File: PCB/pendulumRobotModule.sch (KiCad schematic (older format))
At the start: 24 parts, among them J1 Conn_01x02_Female, J2 conn_3x4, J3 Conn_01x02_Male, J4 Conn_01x04_Female, J5 conn_3x3, J7 Conn_01x04_Female, U1 ESP32-devKit, U2 MPU6050-breakout, U3 buckConverter-adj

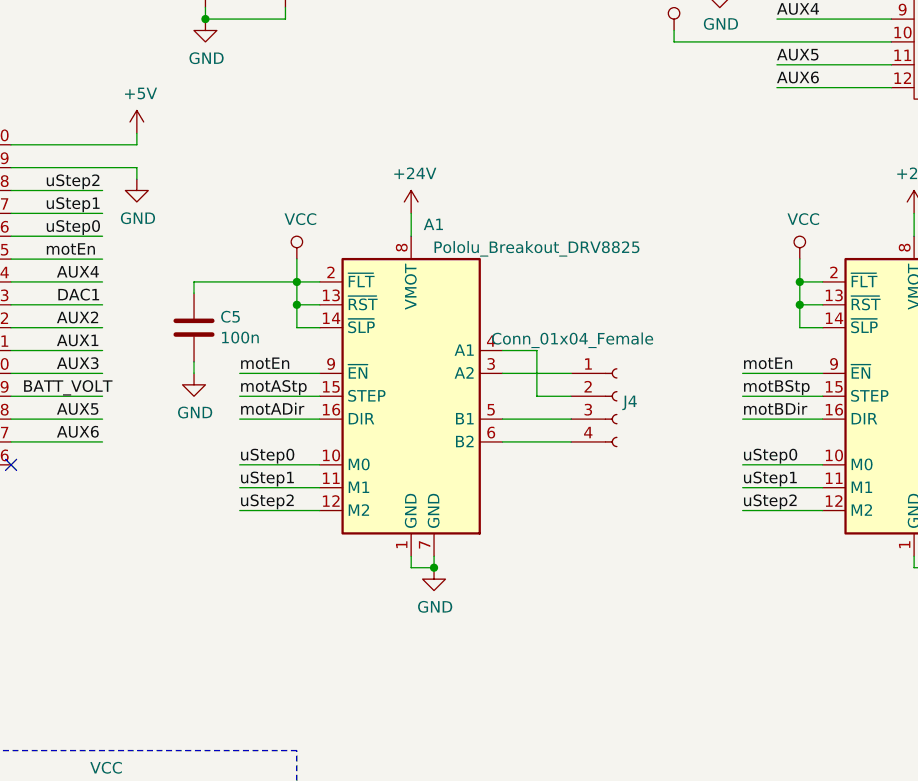
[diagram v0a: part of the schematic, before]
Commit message: PCB updates: increased 24V trace thickness, added a via (or rather added trace to via) in that signal, and added stepper motor enable pull-up to 3V3.
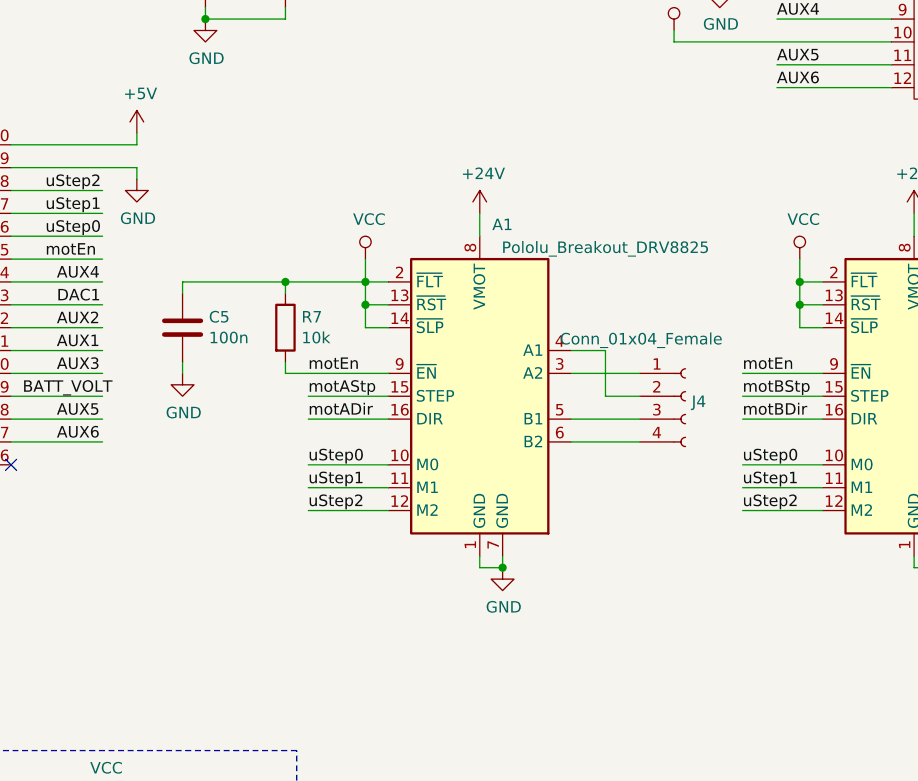
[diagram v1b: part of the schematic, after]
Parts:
- added R7: 10k, Resistors_SMD:R_0805_HandSoldering, symbol Device:R
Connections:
- wire segments 168 -> 171
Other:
- moved on the sheet: A1, C5, J4
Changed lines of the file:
@@
 L Driver_Motor:Pololu_Breakout_DRV8825 A1
 U 1 1 5BCC947E
-P 5500 4300
-F 0 "A1" H 5600 4950 50  0000 C CNN
-F 1 "Pololu_Breakout_DRV8825" H 6050 4850 50  0000 C CNN
-F 2 "mylib:DRV8825-breakout" H 5700 3500 50  0001 L CNN
-F 3 "https://www.pololu.com/product/2982" H 5600 4000 50  0001 C CNN
-	1    5500 4300
+P 5800 4300
+F 0 "A1" H 5900 4950 50  0000 C CNN
+F 1 "Pololu_Breakout_DRV8825" H 6350 4850 50  0000 C CNN
+F 2 "mylib:DRV8825-breakout" H 6000 3500 50  0001 L CNN
+F 3 "https://www.pololu.com/product/2982" H 5900 4000 50  0001 C CNN
+	1    5800 4300
 	1    0    0    -1
 $EndComp
@@
 L Connector:Conn_01x04_Female J4
 U 1 1 5BCCD4CD
-P 6400 4400
-F 0 "J4" H 6427 4376 50  0000 L CNN
-F 1 "Conn_01x04_Female" H 5850 4650 50  0000 L CNN
-F 2 "Socket_Strips:Socket_Strip_Straight_1x04_Pitch2.54mm" H 6400 4400 50  0001 C CNN
-F 3 "~" H 6400 4400 50  0001 C CNN
-	1    6400 4400
+P 6700 4400
+F 0 "J4" H 6727 4376 50  0000 L CNN
+F 1 "Conn_01x04_Female" H 6150 4650 50  0000 L CNN
+F 2 "Socket_Strips:Socket_Strip_Straight_1x04_Pitch2.54mm" H 6700 4400 50  0001 C CNN
+F 3 "~" H 6700 4400 50  0001 C CNN
+	1    6700 4400
 	1    0    0    -1
 $EndComp
@@
 	1    0    0    -1
 $EndComp
-Text Label 4750 4700 0    50   ~ 0
+Text Label 5050 4700 0    50   ~ 0
 uStep0
-Text Label 4750 4800 0    50   ~ 0
+Text Label 5050 4800 0    50   ~ 0
 uStep1
-Text Label 4750 4900 0    50   ~ 0
+Text Label 5050 4900 0    50   ~ 0
 uStep2
 Text Label 6950 4700 0    50   ~ 0
@@
 Text Label 6950 4300 0    50   ~ 0
 motEn
-Text Label 4750 4300 0    50   ~ 0
+Text Label 5050 4300 0    50   ~ 0
 motEn
 $Comp
 L power:GND #PWR0112
 U 1 1 5BD07181
-P 5600 5150
-F 0 "#PWR0112" H 5600 4900 50  0001 C CNN
-F 1 "GND" H 5605 4977 50  0000 C CNN
-F 2 "" H 5600 5150 50  0001 C CNN
-F 3 "" H 5600 5150 50  0001 C CNN
-	1    5600 5150
-	1    0    0    -1
-$EndComp
-Wire Wire Line
-	5500 5100 5500 5150
-Wire Wire Line
-	5500 5150 5600 5150
-Wire Wire Line
-	5600 5100 5600 5150
-Connection ~ 5600 5150
+P 5900 5150
+F 0 "#PWR0112" H 5900 4900 50  0001 C CNN
+F 1 "GND" H 5905 4977 50  0000 C CNN
+F 2 "" H 5900 5150 50  0001 C CNN
+F 3 "" H 5900 5150 50  0001 C CNN
+	1    5900 5150
+	1    0    0    -1
+$EndComp
+Wire Wire Line
+	5800 5100 5800 5150
+Wire Wire Line
+	5800 5150 5900 5150
+Wire Wire Line
+	5900 5100 5900 5150
+Connection ~ 5900 5150
 $Comp
 L power:GND #PWR0113
@@
 L power:+24V #PWR0114
 U 1 1 5BD122E8
-P 5500 3600
-F 0 "#PWR0114" H 5500 3450 50  0001 C CNN
-F 1 "+24V" H 5515 3773 50  0000 C CNN
-F 2 "" H 5500 3600 50  0001 C CNN
-F 3 "" H 5500 3600 50  0001 C CNN
-	1    5500 3600
+P 5800 3600
+F 0 "#PWR0114" H 5800 3450 50  0001 C CNN
+F 1 "+24V" H 5815 3773 50  0000 C CNN
+F 2 "" H 5800 3600 50  0001 C CNN
+F 3 "" H 5800 3600 50  0001 C CNN
+	1    5800 3600
 	1    0    0    -1
 $EndComp
@@
 $EndComp
 Wire Wire Line
-	5500 3600 5500 3700
+	5800 3600 5800 3700
 Wire Wire Line
 	7700 3600 7700 3700
-Text Label 4750 4500 0    50   ~ 0
+Text Label 5050 4500 0    50   ~ 0
 motADir
 Wire Wire Line
-	4750 4400 5100 4400
-Wire Wire Line
-	4750 4300 5100 4300
-Wire Wire Line
-	5100 4500 4750 4500
-Wire Wire Line
-	4750 4700 5100 4700
-Wire Wire Line
-	4750 4800 5100 4800
-Wire Wire Line
-	4750 4900 5100 4900
-Text Label 4750 4400 0    50   ~ 0
+	5050 4400 5400 4400
+Wire Wire Line
+	5400 4500 5050 4500
+Wire Wire Line
+	5050 4700 5400 4700
+Wire Wire Line
+	5050 4800 5400 4800
+Wire Wire Line
+	5050 4900 5400 4900
+Text Label 5050 4400 0    50   ~ 0
 motAStp
 $Comp
 L power:VCC #PWR0116
 U 1 1 5BD29F29
-P 5000 3800
-F 0 "#PWR0116" H 5000 3650 50  0001 C CNN
-F 1 "VCC" H 5017 3973 50  0000 C CNN
-F 2 "" H 5000 3800 50  0001 C CNN
-F 3 "" H 5000 3800 50  0001 C CNN
-	1    5000 3800
-	1    0    0    -1
-$EndComp
-Wire Wire Line
-	5100 3900 5000 3900
-Wire Wire Line
-	5000 3900 5000 3800
-Wire Wire Line
-	5100 4000 5000 4000
-Wire Wire Line
-	5000 4000 5000 3900
-Connection ~ 5000 3900
-Wire Wire Line
-	5100 4100 5000 4100
-Wire Wire Line
-	5000 4100 5000 4000
-Connection ~ 5000 4000
+P 5300 3800
+F 0 "#PWR0116" H 5300 3650 50  0001 C CNN
+F 1 "VCC" H 5317 3973 50  0000 C CNN
+F 2 "" H 5300 3800 50  0001 C CNN
+F 3 "" H 5300 3800 50  0001 C CNN
+	1    5300 3800
+	1    0    0    -1
+$EndComp
+Wire Wire Line
+	5400 3900 5300 3900
+Wire Wire Line
+	5300 3900 5300 3800
+Wire Wire Line
+	5400 4000 5300 4000
+Wire Wire Line
+	5300 4000 5300 3900
+Connection ~ 5300 3900
+Wire Wire Line
+	5400 4100 5300 4100
+Wire Wire Line
+	5300 4100 5300 4000
+Connection ~ 5300 4000
 $Comp
 L power:VCC #PWR0117
@@
 	1650 2250 1650 2350
 Wire Wire Line
-	5900 4600 6200 4600
-Wire Wire Line
-	5900 4500 6200 4500
-Wire Wire Line
-	5900 4300 6200 4300
-Wire Wire Line
-	5900 4200 6050 4200
-Wire Wire Line
-	6050 4200 6050 4400
-Wire Wire Line
-	6050 4400 6200 4400
+	6200 4600 6500 4600
+Wire Wire Line
+	6200 4500 6500 4500
+Wire Wire Line
+	6200 4300 6500 4300
+Wire Wire Line
+	6200 4200 6350 4200
+Wire Wire Line
+	6350 4200 6350 4400
+Wire Wire Line
+	6350 4400 6500 4400
 Wire Wire Line
 	8100 4600 8400 4600
@@
 L Device:C C5
 U 1 1 5BD75DEB
-P 4550 4100
-F 0 "C5" H 4665 4146 50  0000 L CNN
-F 1 "100n" H 4665 4055 50  0000 L CNN
-F 2 "Capacitors_SMD:C_0805_HandSoldering" H 4588 3950 50  0001 C CNN
-F 3 "~" H 4550 4100 50  0001 C CNN
-	1    4550 4100
-	1    0    0    -1
-$EndComp
-Wire Wire Line
-	5000 3900 4550 3900
-Wire Wire Line
-	4550 3900 4550 3950
+P 4500 4100
+F 0 "C5" H 4615 4146 50  0000 L CNN
+F 1 "100n" H 4615 4055 50  0000 L CNN
+F 2 "Capacitors_SMD:C_0805_HandSoldering" H 4538 3950 50  0001 C CNN
+F 3 "~" H 4500 4100 50  0001 C CNN
+	1    4500 4100
+	1    0    0    -1
+$EndComp
+Wire Wire Line
+	4950 3900 4500 3900
+Wire Wire Line
+	4500 3900 4500 3950
 $Comp
 L power:GND #PWR0126
 U 1 1 5BD7D24B
-P 4550 4300
-F 0 "#PWR0126" H 4550 4050 50  0001 C CNN
-F 1 "GND" H 4555 4127 50  0000 C CNN
-F 2 "" H 4550 4300 50  0001 C CNN
-F 3 "" H 4550 4300 50  0001 C CNN
-	1    4550 4300
-	1    0    0    -1
-$EndComp
-Wire Wire Line
-	4550 4250 4550 4300
+P 4500 4300
+F 0 "#PWR0126" H 4500 4050 50  0001 C CNN
+F 1 "GND" H 4505 4127 50  0000 C CNN
+F 2 "" H 4500 4300 50  0001 C CNN
+F 3 "" H 4500 4300 50  0001 C CNN
+	1    4500 4300
+	1    0    0    -1
+$EndComp
+Wire Wire Line
+	4500 4250 4500 4300
 Connection ~ 9100 4250
 Wire Wire Line
@@
 	9050 4950 9050 4750
 Connection ~ 9050 4750
+$Comp
+L Device:R R7
+U 1 1 5BE75466
+P 4950 4100
+F 0 "R7" H 5020 4146 50  0000 L CNN
+F 1 "10k" H 5020 4055 50  0000 L CNN
+F 2 "Resistors_SMD:R_0805_HandSoldering" V 4880 4100 50  0001 C CNN
+F 3 "~" H 4950 4100 50  0001 C CNN
+	1    4950 4100
+	1    0    0    -1
+$EndComp
+Wire Wire Line
+	4950 4300 4950 4250
+Wire Wire Line
+	4950 4300 5400 4300
+Wire Wire Line
+	4950 3900 4950 3950
+Wire Wire Line
+	4950 3900 5300 3900
+Connection ~ 4950 3900
 $EndSCHEMATC

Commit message: Changed 10uF cap to 1uF. Also, changed text on bottom layer to point to the correct reposityor.
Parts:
- C3: value 10u -> 1u
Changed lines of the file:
@@
 P 4950 2550
 F 0 "C3" H 5065 2596 50  0000 L CNN
-F 1 "10u" H 5065 2505 50  0000 L CNN
+F 1 "1u" H 5065 2505 50  0000 L CNN
 F 2 "Capacitors_SMD:C_0805_HandSoldering" H 4988 2400 50  0001 C CNN
 F 3 "~" H 4950 2550 50  0001 C CNN

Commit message: Updated PCB readme.
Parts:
- R7: value 10k -> 3k3
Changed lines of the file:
@@
 P 4950 4100
 F 0 "R7" H 5020 4146 50  0000 L CNN
-F 1 "10k" H 5020 4055 50  0000 L CNN
+F 1 "3k3" H 5020 4055 50  0000 L CNN
 F 2 "Resistors_SMD:R_0805_HandSoldering" V 4880 4100 50  0001 C CNN
 F 3 "~" H 4950 4100 50  0001 C CNN

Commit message: PCB updated to version 1.2: added RX pulldown resistor and 5V buffer capacitor (both optional). Added some markings for buck converter. Web interface now has a fancy option for logging data (plotTest.htm)
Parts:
- added C6: 470u, Capacitors_THT:CP_Radial_D6.3mm_P2.50mm, symbol Device:CP
- added J6: Conn_01x02_Male, mylib:pinHeader_2x1_5.08mm, symbol Connector:Conn_01x02_Male
- added R8: 100k, Resistors_SMD:R_0805_HandSoldering, symbol Device:R
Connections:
- wire segments 171 -> 178
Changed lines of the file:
@@
 Text Label 1450 4200 0    50   ~ 0
 SERVO_PWM
-Wire Wire Line
-	1950 3800 1450 3800
 Text Label 1450 3800 0    50   ~ 0
 IBUS_RX
@@
 	4950 3900 5300 3900
 Connection ~ 4950 3900
+$Comp
+L Device:R R8
+U 1 1 5C596ABB
+P 1150 4050
+F 0 "R8" H 1220 4096 50  0000 L CNN
+F 1 "100k" H 1220 4005 50  0000 L CNN
+F 2 "Resistors_SMD:R_0805_HandSoldering" V 1080 4050 50  0001 C CNN
+F 3 "~" H 1150 4050 50  0001 C CNN
+	1    1150 4050
+	1    0    0    -1
+$EndComp
+$Comp
+L power:GND #PWR02
+U 1 1 5C596B33
+P 1150 4250
+F 0 "#PWR02" H 1150 4000 50  0001 C CNN
+F 1 "GND" H 1155 4077 50  0000 C CNN
+F 2 "" H 1150 4250 50  0001 C CNN
+F 3 "" H 1150 4250 50  0001 C CNN
+	1    1150 4250
+	1    0    0    -1
+$EndComp
+Wire Wire Line
+	1150 4250 1150 4200
+Wire Wire Line
+	1150 3900 1150 3800
+Wire Wire Line
+	1150 3800 1950 3800
+$Comp
+L Device:CP C6
+U 1 1 5C5A6BE2
+P 6150 2150
+F 0 "C6" H 6268 2196 50  0000 L CNN
+F 1 "470u" H 6268 2105 50  0000 L CNN
+F 2 "Capacitors_THT:CP_Radial_D6.3mm_P2.50mm" H 6188 2000 50  0001 C CNN
+F 3 "~" H 6150 2150 50  0001 C CNN
+	1    6150 2150
+	1    0    0    -1
+$EndComp
+$Comp
+L power:GND #PWR03
+U 1 1 5C5A6C84
+P 6150 2300
+F 0 "#PWR03" H 6150 2050 50  0001 C CNN
+F 1 "GND" H 6155 2127 50  0000 C CNN
+F 2 "" H 6150 2300 50  0001 C CNN
+F 3 "" H 6150 2300 50  0001 C CNN
+	1    6150 2300
+	1    0    0    -1
+$EndComp
+Wire Wire Line
+	6150 2000 6150 1950
+Connection ~ 6150 1950
+$Comp
+L Connector:Conn_01x02_Male J6
+U 1 1 5C5AF1E1
+P 2500 2650
+F 0 "J6" H 2606 2828 50  0000 C CNN
+F 1 "Conn_01x02_Male" H 2606 2737 50  0000 C CNN
+F 2 "mylib:pinHeader_2x1_5.08mm" H 2500 2650 50  0001 C CNN
+F 3 "~" H 2500 2650 50  0001 C CNN
+	1    2500 2650
+	1    0    0    -1
+$EndComp
+$Comp
+L power:+24V #PWR04
+U 1 1 5C5AF287
+P 3050 2600
+F 0 "#PWR04" H 3050 2450 50  0001 C CNN
+F 1 "+24V" H 3065 2773 50  0000 C CNN
+F 2 "" H 3050 2600 50  0001 C CNN
+F 3 "" H 3050 2600 50  0001 C CNN
+	1    3050 2600
+	1    0    0    -1
+$EndComp
+$Comp
+L power:GND #PWR05
+U 1 1 5C5AF2CA
+P 3050 2800
+F 0 "#PWR05" H 3050 2550 50  0001 C CNN
+F 1 "GND" H 3055 2627 50  0000 C CNN
+F 2 "" H 3050 2800 50  0001 C CNN
+F 3 "" H 3050 2800 50  0001 C CNN
+	1    3050 2800
+	1    0    0    -1
+$EndComp
+Wire Wire Line
+	2700 2750 3050 2750
+Wire Wire Line
+	3050 2750 3050 2800
+Wire Wire Line
+	3050 2650 3050 2600
+Wire Wire Line
+	2700 2650 3050 2650
 $EndSCHEMATC

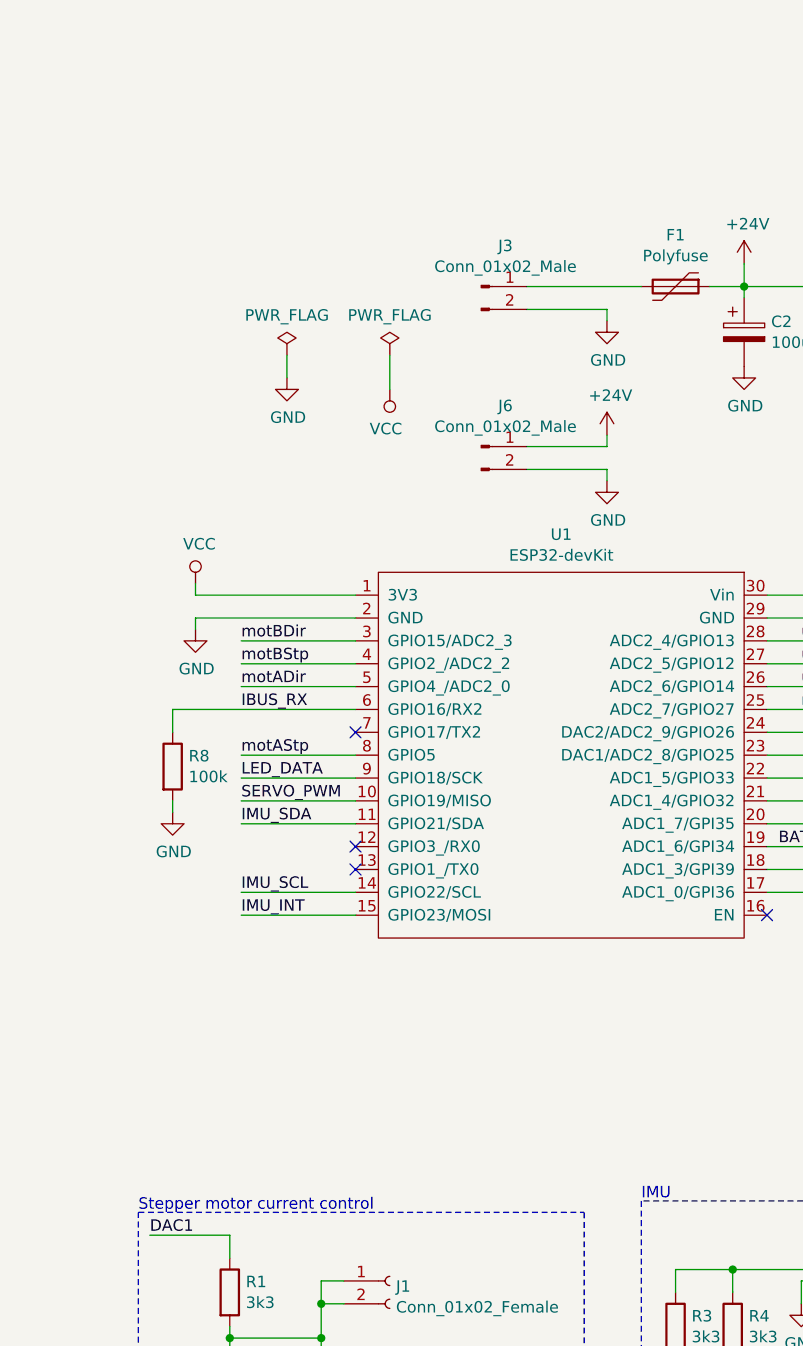
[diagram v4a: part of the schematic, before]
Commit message: PCB v1.3 update. Added power switch, battery connector, and status LEDs.
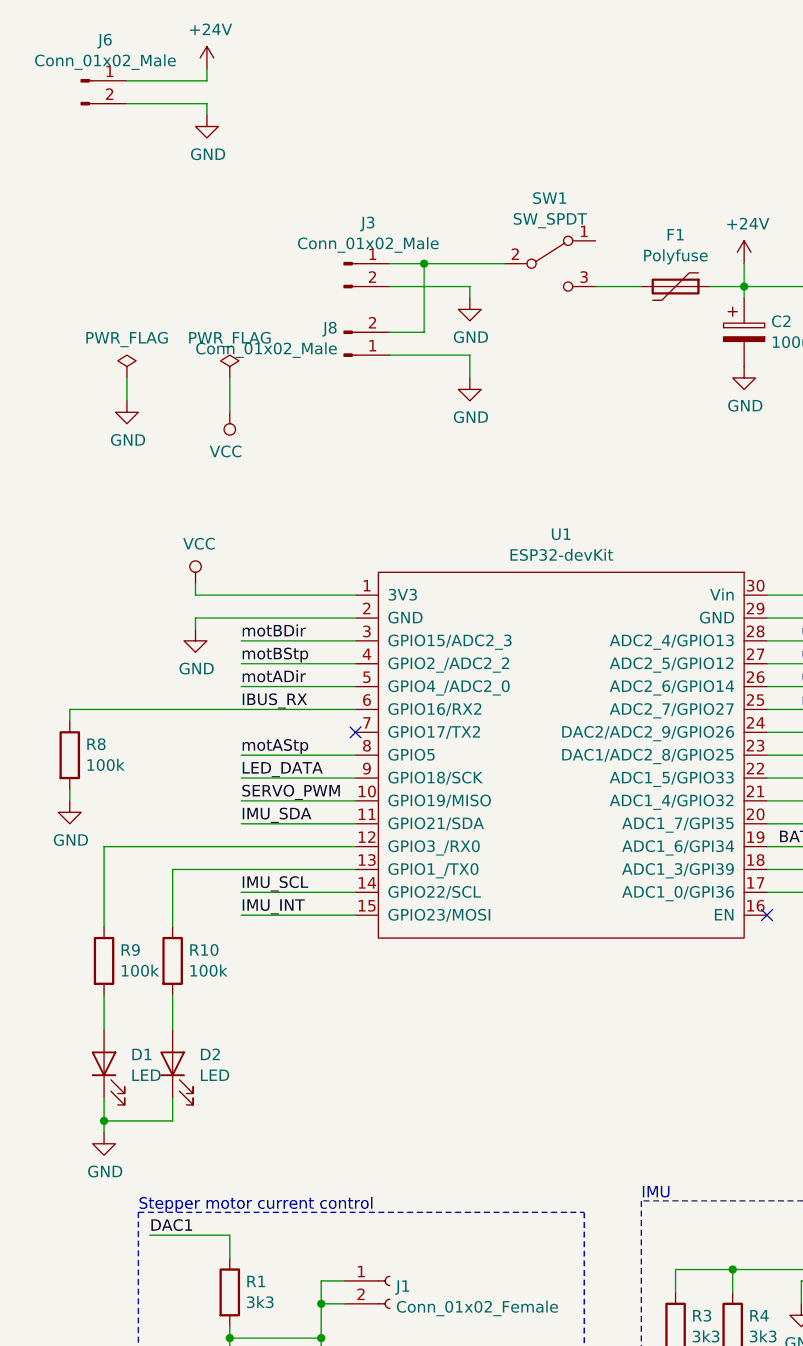
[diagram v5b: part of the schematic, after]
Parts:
- added D1, D2: LED, LED_THT:LED_D5.0mm, symbol Device:LED
- added J8: Conn_01x02_Male, Connector_JST:JST_XH_S02B-XH-A-1_1x02_P2.50mm_Horizontal, symbol Connector:Conn_01x02_Male
- added R10, R9: 100k, Resistors_SMD:R_0805_HandSoldering, symbol Device:R
- added SW1: SW_SPDT, mylib:switch_slider_SPDT_angled, symbol Switch:SW_SPDT
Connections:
- wire segments 178 -> 194
- no-connect marks 6 -> 4
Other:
- moved on the sheet: J3, J6, R8
